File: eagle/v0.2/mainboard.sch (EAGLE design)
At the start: 32 parts, among them J1 12401832E402A, J2 12401832E402A, J3 12401832E402A, J4 12401832E402A, J5 12401832E402A, J7 L77HDE15SD1CH4RHNVGA

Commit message: added mainboard controller logic
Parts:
- added IC1, IC2, IC3, IC4, IC5, IC6: 74HCT151D, 74xx-eu:74HCT151D
- added IC7: 74HC590D, 74xx-eu:74HC590D
- added IC8: 74HC02D, 74xx-eu:74HC02D
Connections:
- new net C1-C4: IC5A.Y
- new net N$10: IC1A.B, IC2A.B, IC3A.B, IC4A.B, IC5A.B, IC7A.QB
- new net N$11: IC1A.C, IC2A.C, IC3A.C, IC4A.C, IC5A.C, IC7A.QC
- new net N$12: IC2A.Y, IC6A.D1
- new net N$13: IC1A.Y, IC6A.D0
- new net N$14: IC3A.Y, IC6A.D2
- new net N$15: IC4A.Y, IC6A.D3
- new net N$16: IC5A.D4
- new net N$17: IC5A.G, IC8A.O
- new net N$19: IC6A.B, IC7A.QE, IC8A.I1
- new net N$20: IC5A.W
- new net N$22: IC6A.W
- new net N$24: IC6A.A, IC7A.QD, IC8A.I0
- new net N$61: IC7A.CLK, IC7A.RCK
- new net N$65: IC5A.D3
- new net N$66: IC5A.D2
- new net N$67: IC5A.D1
- new net N$9: IC1A.A, IC2A.A, IC3A.A, IC4A.A, IC5A.A, IC7A.QA
- new net SYNC: IC6A.Y
- net +5V: now also IC5A.D0, IC7A.CCLR
- net C1_A: now also IC1A.D7
- net C1_B: now also IC1A.D6
- net C1_DOWN: now also IC1A.D2
- net C1_LEFT: now also IC1A.D1
- net C1_RIGHT: now also IC1A.D0
- net C1_SELECT: now also IC1A.D4
- net C1_START: now also IC1A.D5
- net C1_UP: now also IC1A.D3
- net C2_A: now also IC2A.D7
- net C2_B: now also IC2A.D6
- net C2_DOWN: now also IC2A.D2
- net C2_LEFT: now also IC2A.D1
- net C2_RIGHT: now also IC2A.D0
- net C2_SELECT: now also IC2A.D4
- net C2_START: now also IC2A.D5
- net C2_UP: now also IC2A.D3
- net C3_A: now also IC3A.D7
- net C3_B: now also IC3A.D6
- net C3_DOWN: now also IC3A.D2
- net C3_LEFT: now also IC3A.D1
- net C3_RIGHT: now also IC3A.D0
- net C3_SELECT: now also IC3A.D4
- net C3_START: now also IC3A.D5
- net C3_UP: now also IC3A.D3
- net C4_A: now also IC4A.D7
- net C4_B: now also IC4A.D6
- net C4_DOWN: now also IC4A.D2
- net C4_LEFT: now also IC4A.D1
- net C4_RIGHT: now also IC4A.D0
- net C4_SELECT: now also IC4A.D4
- net C4_START: now also IC4A.D5
- net C4_UP: now also IC4A.D3
- net GND: now also IC1A.G, IC2A.G, IC3A.G, IC4A.G, IC5A.D5, IC5A.D6, IC5A.D7, IC6A.C, IC6A.D4, IC6A.D5, IC6A.D6, IC6A.D7, IC6A.G, IC7A.CCKEN, IC7A.G, IC8B.I0, IC8B.I1, IC8C.I0, IC8C.I1, IC8D.I0, IC8D.I1

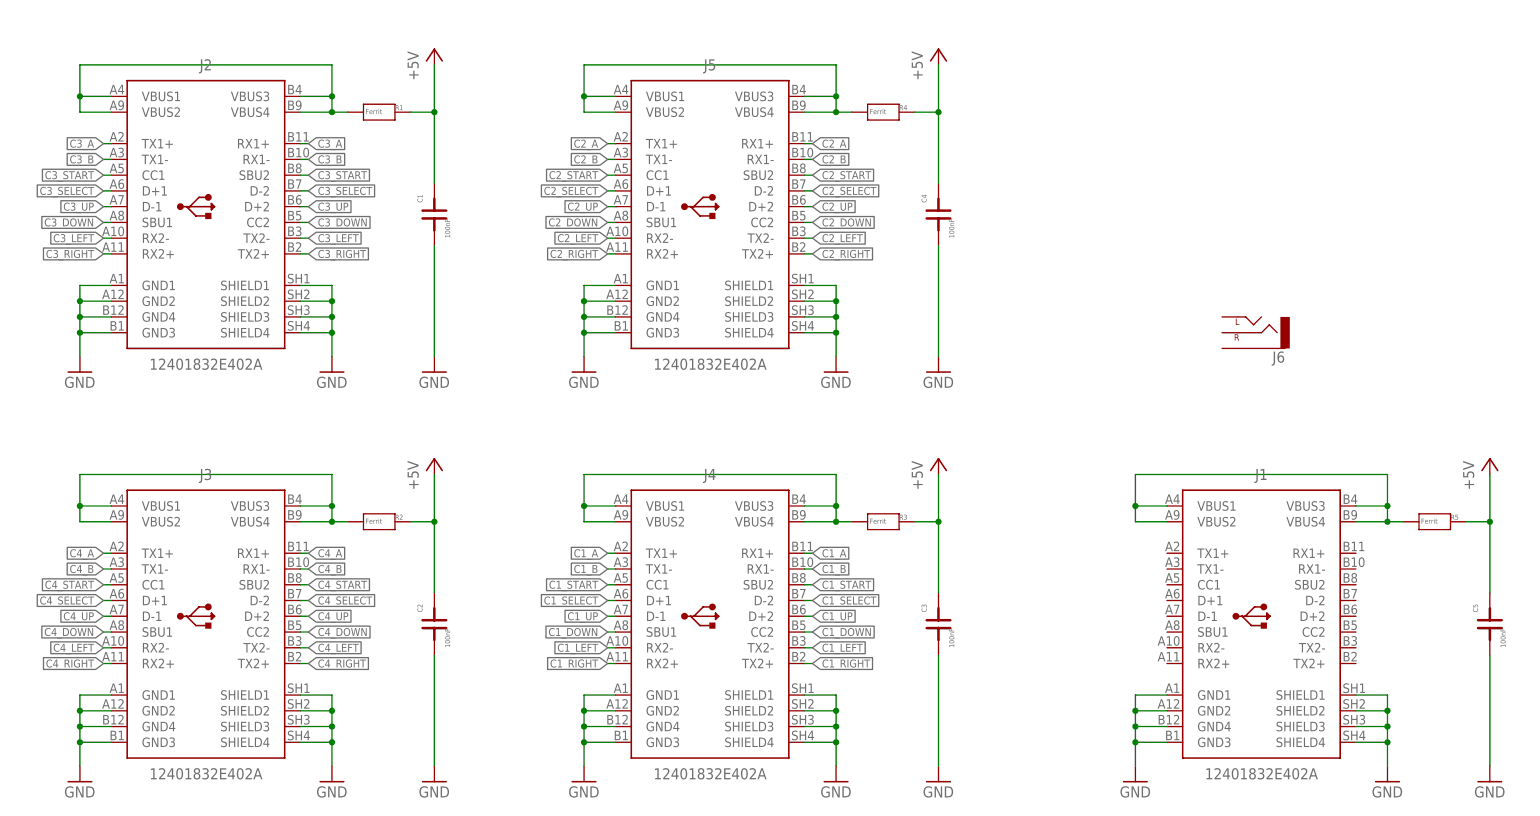
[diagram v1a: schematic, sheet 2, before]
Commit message: mainboard controller schematic
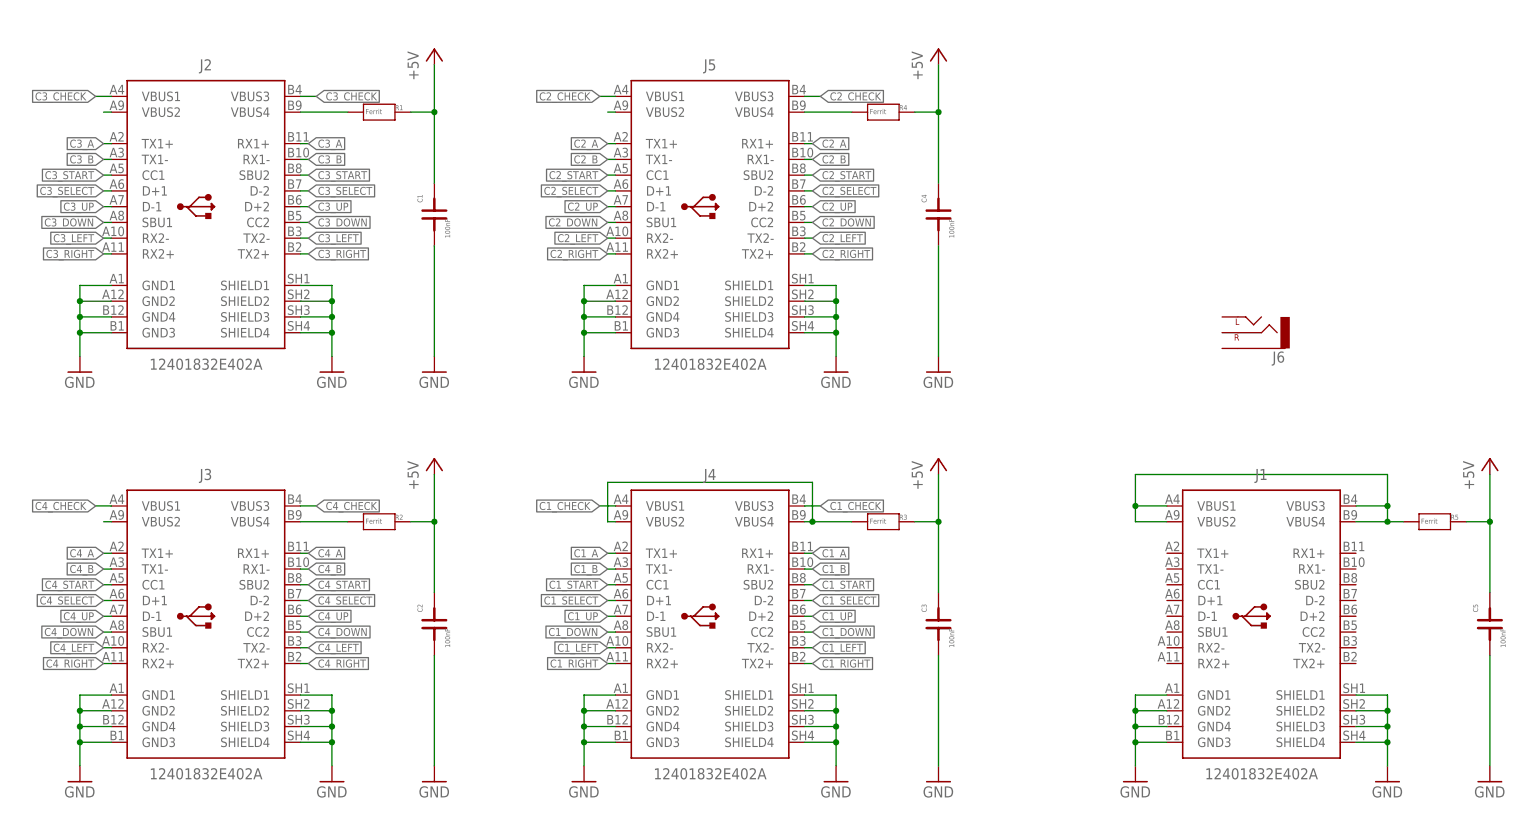
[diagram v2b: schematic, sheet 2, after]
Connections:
- removed net C1-C4: IC5A.Y
- removed net N$16: IC5A.D4
- removed net N$2: J3.VBUS1, J3.VBUS2, J3.VBUS3, J3.VBUS4, R2.1
- removed net N$65: IC5A.D3
- removed net N$66: IC5A.D2
- removed net N$67: IC5A.D1
- new net C1_CHECK: IC5A.D1, J4.VBUS1, J4.VBUS3
- new net C2_CHECK: IC5A.D2, J5.VBUS1, J5.VBUS3
- new net C3_CHECK: IC5A.D3, J2.VBUS1, J2.VBUS3
- new net C4_CHECK: IC5A.D4, J3.VBUS1, J3.VBUS3
- new net DATA: IC6A.Y
- new net N$21: J3.VBUS2
- new net N$23: J4.VBUS2, J4.VBUS4, R3.1
- new net N$26: J2.VBUS2
- new net N$28: J5.VBUS2
- net N$1: no longer J2.VBUS1, J2.VBUS2, J2.VBUS3
- net N$4: now also J3.VBUS4, R2.1; no longer J4.VBUS1, J4.VBUS2, J4.VBUS3, J4.VBUS4, R3.1
- net N$5: no longer J5.VBUS1, J5.VBUS2, J5.VBUS3
- net SYNC: now also IC5A.Y; no longer IC6A.Y
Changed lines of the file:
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@@
 <setting verticaltext="up"/>
 </settings>
-<grid distance="100" unitdist="mil" unit="mil" style="lines" multiple="1" display="yes" altdistance="0.01" altunitdist="inch" altunit="inch"/>
+<grid distance="50" unitdist="mil" unit="mil" style="lines" multiple="1" display="yes" altdistance="0.01" altunitdist="inch" altunit="inch"/>
 <layers>
 <layer number="1" name="Top" color="4" fill="1" visible="no" active="no"/>
@@
 <net name="N$1" class="0">
 <segment>
-<pinref part="J2" gate="G$1" pin="VBUS2"/>
-<wire x1="16.51" y1="160.02" x2="16.51" y2="157.48" width="0.1524" layer="91"/>
-<wire x1="21.59" y1="157.48" x2="16.51" y2="157.48" width="0.1524" layer="91"/>
-<pinref part="J2" gate="G$1" pin="VBUS1"/>
-<wire x1="21.59" y1="160.02" x2="16.51" y2="160.02" width="0.1524" layer="91"/>
-<wire x1="57.15" y1="165.1" x2="16.51" y2="165.1" width="0.1524" layer="91"/>
-<wire x1="16.51" y1="165.1" x2="16.51" y2="160.02" width="0.1524" layer="91"/>
-<junction x="16.51" y="160.02"/>
 <pinref part="J2" gate="G$1" pin="VBUS4"/>
 <pinref part="R1" gate="G$1" pin="1"/>
-<wire x1="52.07" y1="157.48" x2="57.15" y2="157.48" width="0.1524" layer="91"/>
-<wire x1="57.15" y1="157.48" x2="59.69" y2="157.48" width="0.1524" layer="91"/>
-<wire x1="57.15" y1="165.1" x2="57.15" y2="160.02" width="0.1524" layer="91"/>
-<junction x="57.15" y="157.48"/>
-<pinref part="J2" gate="G$1" pin="VBUS3"/>
-<wire x1="57.15" y1="160.02" x2="57.15" y2="157.48" width="0.1524" layer="91"/>
-<wire x1="52.07" y1="160.02" x2="57.15" y2="160.02" width="0.1524" layer="91"/>
-<junction x="57.15" y="160.02"/>
-</segment>
-</net>
-<net name="N$2" class="0">
-<segment>
-<pinref part="J3" gate="G$1" pin="VBUS2"/>
-<wire x1="16.51" y1="93.98" x2="16.51" y2="91.44" width="0.1524" layer="91"/>
-<wire x1="21.59" y1="91.44" x2="16.51" y2="91.44" width="0.1524" layer="91"/>
+<wire x1="52.07" y1="157.48" x2="59.69" y2="157.48" width="0.1524" layer="91"/>
+</segment>
+</net>
+<net name="C4_CHECK" class="0">
+<segment>
 <pinref part="J3" gate="G$1" pin="VBUS1"/>
-<wire x1="21.59" y1="93.98" x2="16.51" y2="93.98" width="0.1524" layer="91"/>
-<wire x1="57.15" y1="99.06" x2="16.51" y2="99.06" width="0.1524" layer="91"/>
-<wire x1="16.51" y1="99.06" x2="16.51" y2="93.98" width="0.1524" layer="91"/>
-<junction x="16.51" y="93.98"/>
-<pinref part="J3" gate="G$1" pin="VBUS4"/>
-<pinref part="R2" gate="G$1" pin="1"/>
-<wire x1="52.07" y1="91.44" x2="57.15" y2="91.44" width="0.1524" layer="91"/>
-<wire x1="57.15" y1="91.44" x2="59.69" y2="91.44" width="0.1524" layer="91"/>
-<wire x1="57.15" y1="99.06" x2="57.15" y2="93.98" width="0.1524" layer="91"/>
-<junction x="57.15" y="91.44"/>
+<wire x1="21.59" y1="93.98" x2="19.05" y2="93.98" width="0.1524" layer="91"/>
+<label x="19.05" y="93.98" size="1.27" layer="95" rot="R180" xref="yes"/>
+</segment>
+<segment>
 <pinref part="J3" gate="G$1" pin="VBUS3"/>
-<wire x1="57.15" y1="93.98" x2="57.15" y2="91.44" width="0.1524" layer="91"/>
-<wire x1="52.07" y1="93.98" x2="57.15" y2="93.98" width="0.1524" layer="91"/>
-<junction x="57.15" y="93.98"/>
-</segment>
-</net>
-<net name="N$4" class="0">
-<segment>
-<pinref part="J4" gate="G$1" pin="VBUS2"/>
-<wire x1="97.79" y1="93.98" x2="97.79" y2="91.44" width="0.1524" layer="91"/>
-<wire x1="102.87" y1="91.44" x2="97.79" y2="91.44" width="0.1524" layer="91"/>
+<wire x1="52.07" y1="93.98" x2="54.61" y2="93.98" width="0.1524" layer="91"/>
+<label x="54.61" y="93.98" size="1.27" layer="95" xref="yes"/>
+</segment>
+</net>
+<net name="C1_CHECK" class="0">
+<segment>
 <pinref part="J4" gate="G$1" pin="VBUS1"/>
-<wire x1="102.87" y1="93.98" x2="97.79" y2="93.98" width="0.1524" layer="91"/>
-<wire x1="138.43" y1="99.06" x2="97.79" y2="99.06" width="0.1524" layer="91"/>
-<wire x1="97.79" y1="99.06" x2="97.79" y2="93.98" width="0.1524" layer="91"/>
-<junction x="97.79" y="93.98"/>
-<pinref part="J4" gate="G$1" pin="VBUS4"/>
-<pinref part="R3" gate="G$1" pin="1"/>
-<wire x1="133.35" y1="91.44" x2="138.43" y2="91.44" width="0.1524" layer="91"/>
-<wire x1="138.43" y1="91.44" x2="140.97" y2="91.44" width="0.1524" layer="91"/>
-<wire x1="138.43" y1="99.06" x2="138.43" y2="93.98" width="0.1524" layer="91"/>
-<junction x="138.43" y="91.44"/>
+<wire x1="102.87" y1="93.98" x2="100.33" y2="93.98" width="0.1524" layer="91"/>
+<label x="100.33" y="93.98" size="1.27" layer="95" rot="R180" xref="yes"/>
+</segment>
+<segment>
 <pinref part="J4" gate="G$1" pin="VBUS3"/>
-<wire x1="138.43" y1="93.98" x2="138.43" y2="91.44" width="0.1524" layer="91"/>
-<wire x1="133.35" y1="93.98" x2="138.43" y2="93.98" width="0.1524" layer="91"/>
-<junction x="138.43" y="93.98"/>
+<wire x1="133.35" y1="93.98" x2="135.89" y2="93.98" width="0.1524" layer="91"/>
+<label x="135.89" y="93.98" size="1.27" layer="95" xref="yes"/>
 </segment>
 </net>
 <net name="N$5" class="0">
 <segment>
-<pinref part="J5" gate="G$1" pin="VBUS2"/>
-<wire x1="97.79" y1="160.02" x2="97.79" y2="157.48" width="0.1524" layer="91"/>
-<wire x1="102.87" y1="157.48" x2="97.79" y2="157.48" width="0.1524" layer="91"/>
-<pinref part="J5" gate="G$1" pin="VBUS1"/>
-<wire x1="102.87" y1="160.02" x2="97.79" y2="160.02" width="0.1524" layer="91"/>
-<wire x1="138.43" y1="165.1" x2="97.79" y2="165.1" width="0.1524" layer="91"/>
-<wire x1="97.79" y1="165.1" x2="97.79" y2="160.02" width="0.1524" layer="91"/>
-<junction x="97.79" y="160.02"/>
 <pinref part="J5" gate="G$1" pin="VBUS4"/>
 <pinref part="R4" gate="G$1" pin="1"/>
-<wire x1="133.35" y1="157.48" x2="138.43" y2="157.48" width="0.1524" layer="91"/>
-<wire x1="138.43" y1="157.48" x2="140.97" y2="157.48" width="0.1524" layer="91"/>
-<wire x1="138.43" y1="165.1" x2="138.43" y2="160.02" width="0.1524" layer="91"/>
-<junction x="138.43" y="157.48"/>
-<pinref part="J5" gate="G$1" pin="VBUS3"/>
-<wire x1="138.43" y1="160.02" x2="138.43" y2="157.48" width="0.1524" layer="91"/>
-<wire x1="133.35" y1="160.02" x2="138.43" y2="160.02" width="0.1524" layer="91"/>
-<junction x="138.43" y="160.02"/>
+<wire x1="133.35" y1="157.48" x2="140.97" y2="157.48" width="0.1524" layer="91"/>
 </segment>
 </net>
@@
 <wire x1="222.25" y1="93.98" x2="227.33" y2="93.98" width="0.1524" layer="91"/>
 <junction x="227.33" y="93.98"/>
+</segment>
+</net>
+<net name="N$23" class="0">
+<segment>
+<pinref part="J4" gate="G$1" pin="VBUS2"/>
+<wire x1="102.87" y1="91.44" x2="101.6" y2="91.44" width="0.1524" layer="91"/>
+<wire x1="101.6" y1="91.44" x2="101.6" y2="97.79" width="0.1524" layer="91"/>
+<pinref part="R3" gate="G$1" pin="1"/>
+<pinref part="J4" gate="G$1" pin="VBUS4"/>
+<wire x1="133.35" y1="91.44" x2="134.62" y2="91.44" width="0.1524" layer="91"/>
+<wire x1="134.62" y1="91.44" x2="140.97" y2="91.44" width="0.1524" layer="91"/>
+<wire x1="101.6" y1="97.79" x2="134.62" y2="97.79" width="0.1524" layer="91"/>
+<wire x1="134.62" y1="97.79" x2="134.62" y2="91.44" width="0.1524" layer="91"/>
+<junction x="134.62" y="91.44"/>
+</segment>
+</net>
+<net name="N$4" class="0">
+<segment>
+<pinref part="R2" gate="G$1" pin="1"/>
+<pinref part="J3" gate="G$1" pin="VBUS4"/>
+<wire x1="52.07" y1="91.44" x2="59.69" y2="91.44" width="0.1524" layer="91"/>
+</segment>
+</net>
+<net name="N$21" class="0">
+<segment>
+<pinref part="J3" gate="G$1" pin="VBUS2"/>
+<wire x1="21.59" y1="91.44" x2="20.32" y2="91.44" width="0.1524" layer="91"/>
+</segment>
+</net>
+<net name="C3_CHECK" class="0">
+<segment>
+<pinref part="J2" gate="G$1" pin="VBUS1"/>
+<wire x1="21.59" y1="160.02" x2="19.05" y2="160.02" width="0.1524" layer="91"/>
+<label x="19.05" y="160.02" size="1.27" layer="95" rot="R180" xref="yes"/>
+</segment>
+<segment>
+<pinref part="J2" gate="G$1" pin="VBUS3"/>
+<wire x1="52.07" y1="160.02" x2="54.61" y2="160.02" width="0.1524" layer="91"/>
+<label x="54.61" y="160.02" size="1.27" layer="95" xref="yes"/>
+</segment>
+</net>
+<net name="N$26" class="0">
+<segment>
+<pinref part="J2" gate="G$1" pin="VBUS2"/>
+<wire x1="21.59" y1="157.48" x2="20.32" y2="157.48" width="0.1524" layer="91"/>
+</segment>
+</net>
+<net name="C2_CHECK" class="0">
+<segment>
+<pinref part="J5" gate="G$1" pin="VBUS1"/>
+<wire x1="102.87" y1="160.02" x2="100.33" y2="160.02" width="0.1524" layer="91"/>
+<label x="100.33" y="160.02" size="1.27" layer="95" rot="R180" xref="yes"/>
+</segment>
+<segment>
+<pinref part="J5" gate="G$1" pin="VBUS3"/>
+<wire x1="133.35" y1="160.02" x2="135.89" y2="160.02" width="0.1524" layer="91"/>
+<label x="135.89" y="160.02" size="1.27" layer="95" xref="yes"/>
+</segment>
+</net>
+<net name="N$28" class="0">
+<segment>
+<pinref part="J5" gate="G$1" pin="VBUS2"/>
+<wire x1="102.87" y1="157.48" x2="101.6" y2="157.48" width="0.1524" layer="91"/>
 </segment>
 </net>
@@
 <net name="SYNC" class="0">
 <segment>
-<pinref part="IC6" gate="A" pin="Y"/>
-<wire x1="142.24" y1="12.7" x2="149.86" y2="12.7" width="0.1524" layer="91"/>
-<label x="149.86" y="12.7" size="1.778" layer="95" xref="yes"/>
-</segment>
-</net>
-<net name="C1-C4" class="0">
-<segment>
 <pinref part="IC5" gate="A" pin="Y"/>
 <wire x1="144.78" y1="-60.96" x2="149.86" y2="-60.96" width="0.1524" layer="91"/>
@@
 </segment>
 </net>
-<net name="N$65" class="0">
+<net name="C3_CHECK" class="0">
 <segment>
 <pinref part="IC5" gate="A" pin="D3"/>
@@
 </segment>
 </net>
-<net name="N$66" class="0">
+<net name="C2_CHECK" class="0">
 <segment>
 <pinref part="IC5" gate="A" pin="D2"/>
@@
 </segment>
 </net>
-<net name="N$67" class="0">
+<net name="C1_CHECK" class="0">
 <segment>
 <pinref part="IC5" gate="A" pin="D1"/>
@@
 </segment>
 </net>
-<net name="N$16" class="0">
+<net name="C4_CHECK" class="0">
 <segment>
 <pinref part="IC5" gate="A" pin="D4"/>
@@
 </segment>
 </net>
+<net name="DATA" class="0">
+<segment>
+<pinref part="IC6" gate="A" pin="Y"/>
+<wire x1="142.24" y1="12.7" x2="149.86" y2="12.7" width="0.1524" layer="91"/>
+<label x="149.86" y="12.7" size="1.778" layer="95" xref="yes"/>
+</segment>
+</net>
